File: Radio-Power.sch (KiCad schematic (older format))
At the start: 17 parts, among them J1 Input, J2 Radio Power, Q1 BS170, Q2 FQP27P06, Q3 BS170, U1 L7805, U2 ATtiny85-20PU

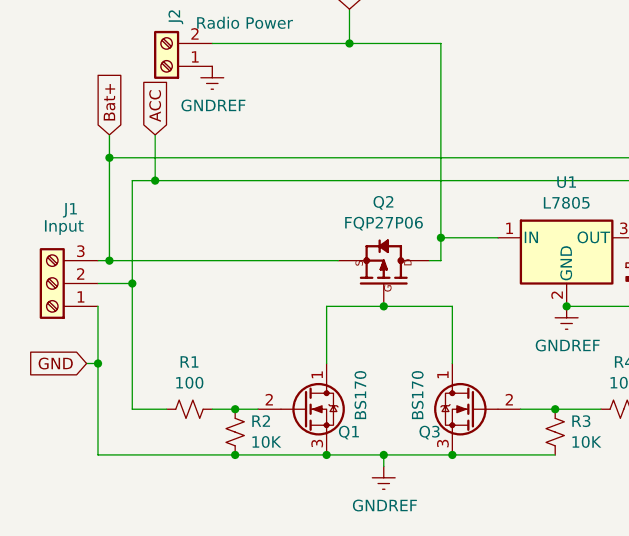
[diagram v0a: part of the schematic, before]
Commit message: Forgot a resistor
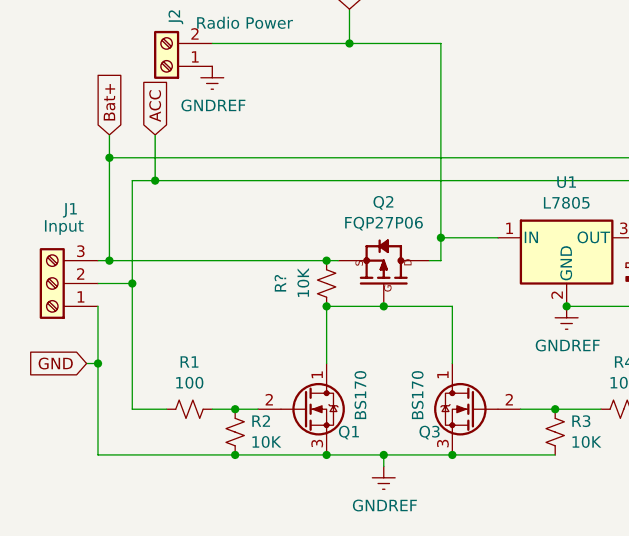
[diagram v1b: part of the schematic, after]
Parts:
- added R?: 10K, Resistor_THT:R_Axial_DIN0207_L6.3mm_D2.5mm_P10.16mm_Horizontal, symbol Device:R_Small_US
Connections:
- net Bat+: now also R?.2
- net at Q1.1 (D), Q2.1 (G), Q3.1 (D): now also R?.1
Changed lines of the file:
@@
 Connection ~ 850  3500
 Wire Wire Line
-	850  3500 1850 3500
+	850  3500 1800 3500
 Wire Wire Line
 	2250 3500 2300 3500
@@
 Wire Wire Line
 	2300 3400 2550 3400
+$Comp
+L Device:R_Small_US R?
+U 1 1 5EABB6D6
+P 1800 3600
+F 0 "R?" V 2000 3600 50  0000 C CNN
+F 1 "10K" V 1900 3600 50  0000 C CNN
+F 2 "Resistor_THT:R_Axial_DIN0207_L6.3mm_D2.5mm_P10.16mm_Horizontal" H 1800 3600 50  0001 C CNN
+F 3 "~" H 1800 3600 50  0001 C CNN
+	1    1800 3600
+	-1   0    0    1
+$EndComp
+Connection ~ 1800 3700
+Connection ~ 1800 3500
+Wire Wire Line
+	1800 3500 1850 3500
 $EndSCHEMATC

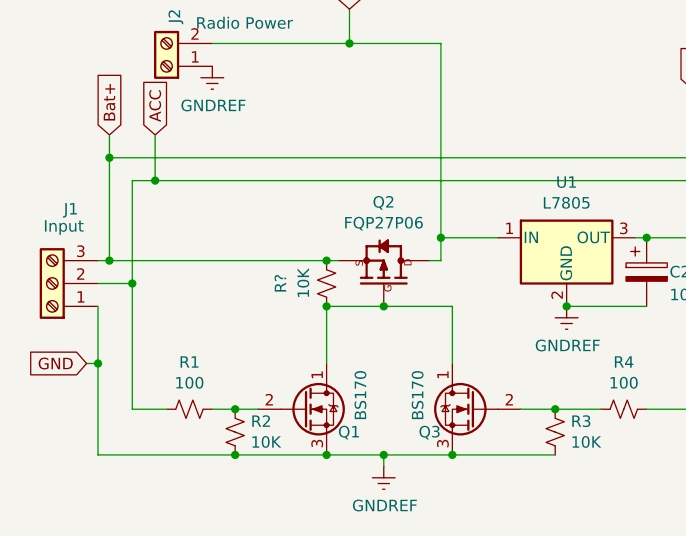
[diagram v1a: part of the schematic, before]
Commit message: Fix rendered schematic
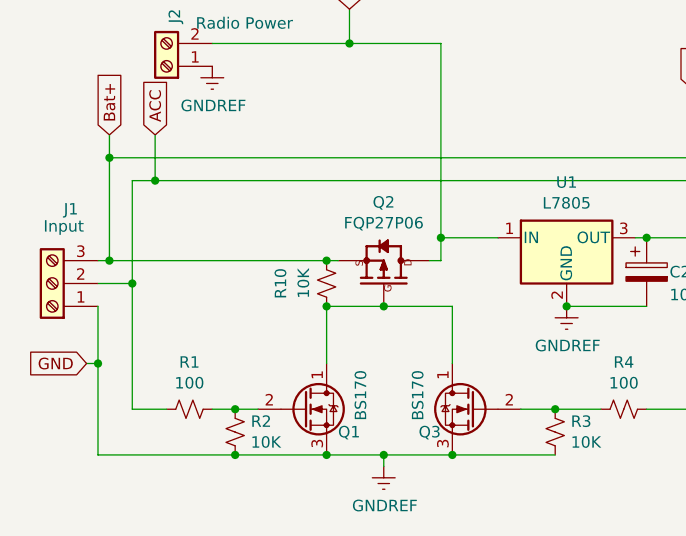
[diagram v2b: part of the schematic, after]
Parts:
- gave numbers to parts that had none: 1
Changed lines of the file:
@@
 	2300 3400 2550 3400
 $Comp
-L Device:R_Small_US R?
+L Device:R_Small_US R10
 U 1 1 5EABB6D6
 P 1800 3600
-F 0 "R?" V 2000 3600 50  0000 C CNN
+F 0 "R10" V 2000 3600 50  0000 C CNN
 F 1 "10K" V 1900 3600 50  0000 C CNN
 F 2 "Resistor_THT:R_Axial_DIN0207_L6.3mm_D2.5mm_P10.16mm_Horizontal" H 1800 3600 50  0001 C CNN

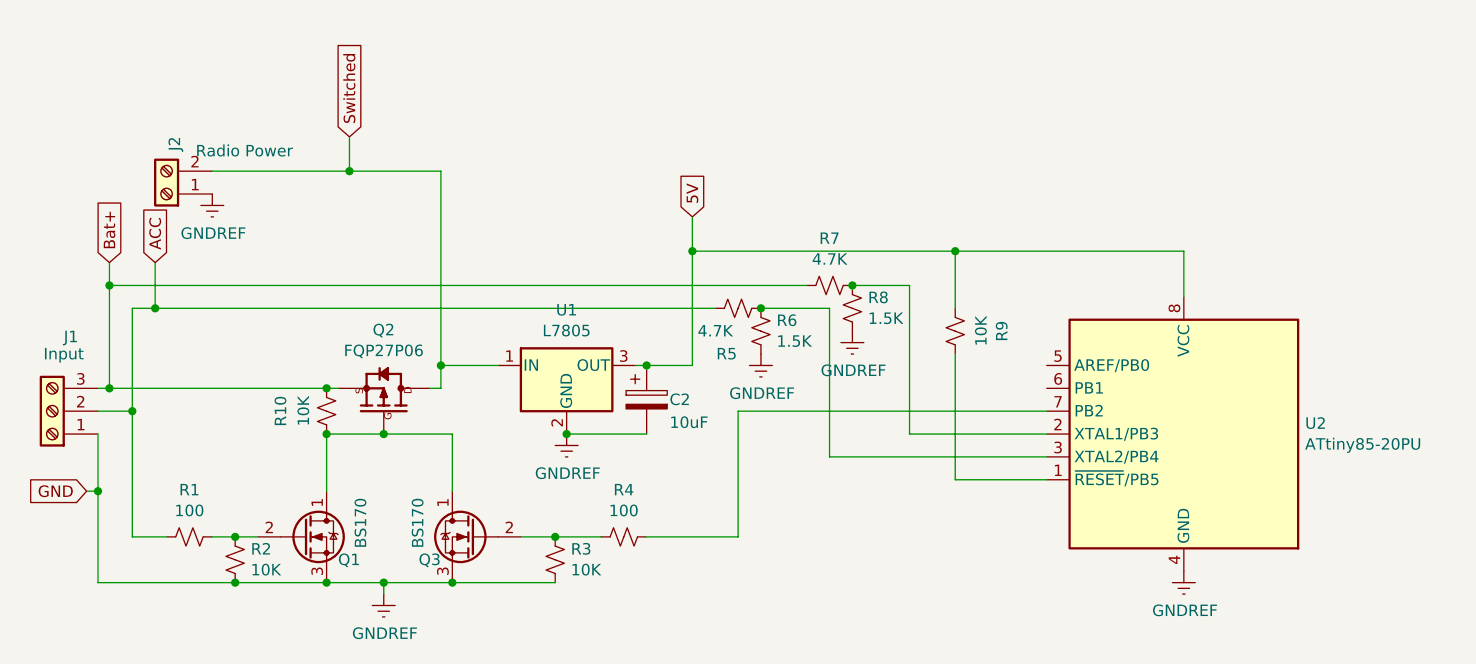
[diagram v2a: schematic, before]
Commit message: Change some things, use switched power for measurement to prevent accidental power flow into the uC
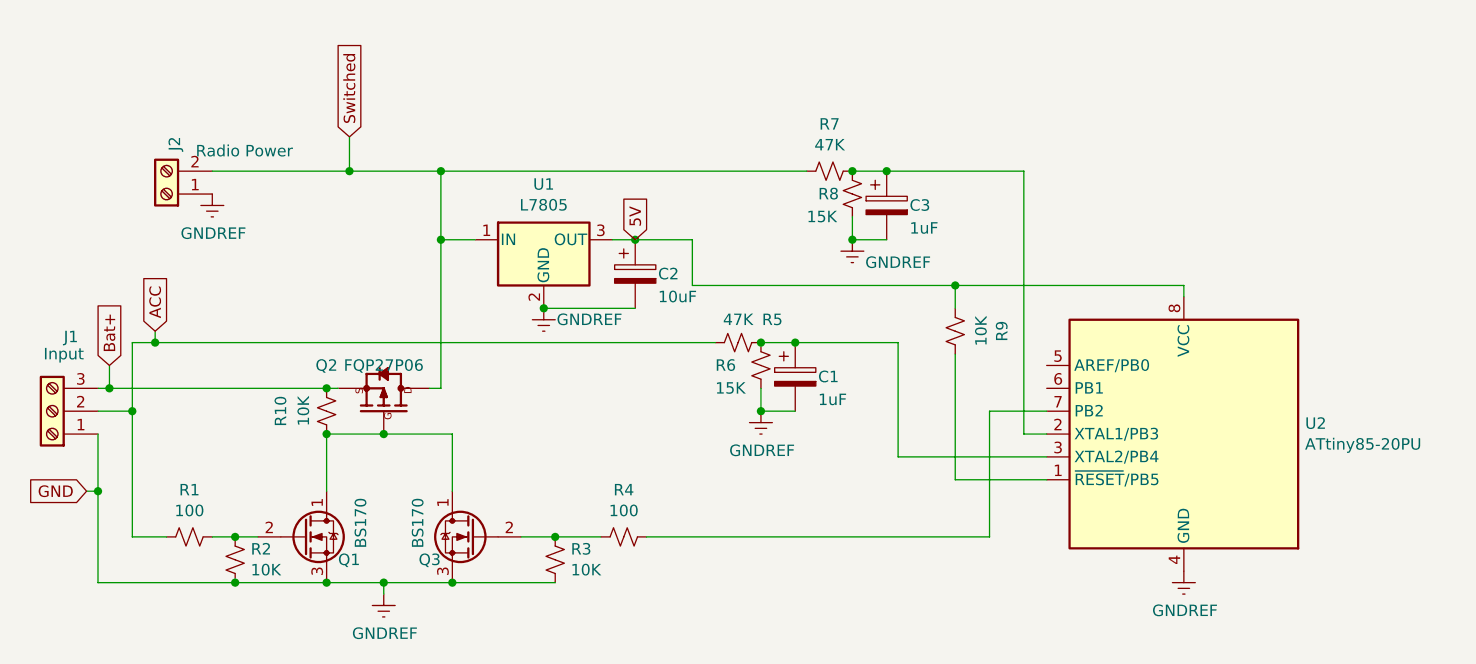
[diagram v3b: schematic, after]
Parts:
- added C1, C3: 1uF, Capacitor_THT:CP_Radial_D4.0mm_P2.00mm, symbol Device:CP
- R5, R7: value 4.7K -> 47K
- R6, R8: value 1.5K -> 15K
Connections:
- net Bat+: no longer R7.2
- net GNDREF: now also C1.2, C3.2
- net Switched: now also R7.2
- net at R7.1, R8.2, U2.2 (XTAL1/PB3): now also C3.1
- net at R5.1, R6.2, U2.3 (XTAL2/PB4): now also C1.1
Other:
- moved on the sheet: C2, R5, R6, R7, R8, U1
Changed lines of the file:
@@
 U 1 1 5EA1FD01
 P 2050 3500
-F 0 "Q2" V 2305 3500 50  0000 C CNN
-F 1 "FQP27P06" V 2214 3500 50  0000 C CNN
+F 0 "Q2" V 2150 3250 50  0000 C CNN
+F 1 "FQP27P06" V 2150 3500 50  0000 C CNN
 F 2 "Package_TO_SOT_THT:TO-220-3_Vertical" H 2050 3500 50  0001 L BNN
 F 3 "67V 27A" H 2050 3500 50  0001 L BNN
@@
 	950  4150 1100 4150
 Wire Wire Line
-	950  3600 950  3150
+	950  3600 950  3300
 Connection ~ 950  3600
-Wire Wire Line
-	850  3500 850  3050
 Connection ~ 850  3500
 Wire Wire Line
@@
 	2250 3500 2300 3500
 Wire Wire Line
-	2300 3500 2300 3400
+	2300 3500 2300 2850
 $Comp
 L MCU_Microchip_ATtiny:ATtiny85-20PU U2
@@
 L Device:R_Small_US R7
 U 1 1 5EA562A8
-P 4000 3050
-F 0 "R7" V 3795 3050 50  0000 C CNN
-F 1 "4.7K" V 3886 3050 50  0000 C CNN
-F 2 "Resistor_THT:R_Axial_DIN0207_L6.3mm_D2.5mm_P10.16mm_Horizontal" H 4000 3050 50  0001 C CNN
-F 3 "~" H 4000 3050 50  0001 C CNN
-	1    4000 3050
+P 4000 2550
+F 0 "R7" V 3795 2550 50  0000 C CNN
+F 1 "47K" V 3886 2550 50  0000 C CNN
+F 2 "Resistor_THT:R_Axial_DIN0207_L6.3mm_D2.5mm_P10.16mm_Horizontal" H 4000 2550 50  0001 C CNN
+F 3 "~" H 4000 2550 50  0001 C CNN
+	1    4000 2550
 	0    1    1    0
 $EndComp
@@
 L Device:R_Small_US R5
 U 1 1 5EA56DEC
-P 3600 3150
-F 0 "R5" V 3800 3100 50  0000 C CNN
-F 1 "4.7K" V 3700 3050 50  0000 C CNN
-F 2 "Resistor_THT:R_Axial_DIN0207_L6.3mm_D2.5mm_P10.16mm_Horizontal" H 3600 3150 50  0001 C CNN
-F 3 "~" H 3600 3150 50  0001 C CNN
-	1    3600 3150
+P 3600 3300
+F 0 "R5" V 3500 3450 50  0000 C CNN
+F 1 "47K" V 3500 3300 50  0000 C CNN
+F 2 "Resistor_THT:R_Axial_DIN0207_L6.3mm_D2.5mm_P10.16mm_Horizontal" H 3600 3300 50  0001 C CNN
+F 3 "~" H 3600 3300 50  0001 C CNN
+	1    3600 3300
 	0    1    1    0
 $EndComp
@@
 L Device:R_Small_US R6
 U 1 1 5EA570DD
-P 3700 3250
-F 0 "R6" H 3632 3204 50  0000 R CNN
-F 1 "1.5K" H 3632 3295 50  0000 R CNN
-F 2 "Resistor_THT:R_Axial_DIN0207_L6.3mm_D2.5mm_P10.16mm_Horizontal" H 3700 3250 50  0001 C CNN
-F 3 "~" H 3700 3250 50  0001 C CNN
-	1    3700 3250
-	-1   0    0    1
-$EndComp
-Wire Wire Line
-	950  3150 1050 3150
-Wire Wire Line
-	850  3050 3900 3050
-Wire Wire Line
-	3700 3150 4000 3150
-Connection ~ 3700 3150
-Wire Wire Line
-	4950 3800 4000 3800
-Wire Wire Line
-	4000 3150 4000 3800
+P 3700 3400
+F 0 "R6" H 3900 3400 50  0000 R CNN
+F 1 "15K" H 3900 3500 50  0000 R CNN
+F 2 "Resistor_THT:R_Axial_DIN0207_L6.3mm_D2.5mm_P10.16mm_Horizontal" H 3700 3400 50  0001 C CNN
+F 3 "~" H 3700 3400 50  0001 C CNN
+	1    3700 3400
+	-1   0    0    1
+$EndComp
+Wire Wire Line
+	950  3300 1050 3300
+Wire Wire Line
+	3700 3300 3850 3300
+Connection ~ 3700 3300
+Wire Wire Line
+	4950 3800 4300 3800
+Wire Wire Line
+	4300 3300 4300 3800
 $Comp
 L Device:R_Small_US R8
 U 1 1 5EA5694E
-P 4100 3150
-F 0 "R8" H 4032 3104 50  0000 R CNN
-F 1 "1.5K" H 4032 3195 50  0000 R CNN
-F 2 "Resistor_THT:R_Axial_DIN0207_L6.3mm_D2.5mm_P10.16mm_Horizontal" H 4100 3150 50  0001 C CNN
-F 3 "~" H 4100 3150 50  0001 C CNN
-	1    4100 3150
-	-1   0    0    1
-$EndComp
-Wire Wire Line
-	4950 3700 4350 3700
-Wire Wire Line
-	4350 3700 4350 3050
-Wire Wire Line
-	4350 3050 4100 3050
-Connection ~ 4100 3050
+P 4100 2650
+F 0 "R8" H 4250 2650 50  0000 R CNN
+F 1 "15K" H 4300 2750 50  0000 R CNN
+F 2 "Resistor_THT:R_Axial_DIN0207_L6.3mm_D2.5mm_P10.16mm_Horizontal" H 4100 2650 50  0001 C CNN
+F 3 "~" H 4100 2650 50  0001 C CNN
+	1    4100 2650
+	-1   0    0    1
+$EndComp
+Wire Wire Line
+	4950 3700 4850 3700
+Wire Wire Line
+	4850 3700 4850 2550
+Wire Wire Line
+	4850 2550 4250 2550
+Connection ~ 4100 2550
 $Comp
 L power:GNDREF #PWR0102
 U 1 1 5EA25084
-P 3700 3350
-F 0 "#PWR0102" H 3700 3100 50  0001 C CNN
-F 1 "GNDREF" H 3705 3177 50  0000 C CNN
-F 2 "" H 3700 3350 50  0001 C CNN
-F 3 "" H 3700 3350 50  0001 C CNN
-	1    3700 3350
+P 3700 3600
+F 0 "#PWR0102" H 3700 3350 50  0001 C CNN
+F 1 "GNDREF" H 3705 3427 50  0000 C CNN
+F 2 "" H 3700 3600 50  0001 C CNN
+F 3 "" H 3700 3600 50  0001 C CNN
+	1    3700 3600
 	1    0    0    -1
 $EndComp
@@
 L power:GNDREF #PWR0103
 U 1 1 5EA2541B
-P 4100 3250
-F 0 "#PWR0103" H 4100 3000 50  0001 C CNN
-F 1 "GNDREF" H 4105 3077 50  0000 C CNN
-F 2 "" H 4100 3250 50  0001 C CNN
-F 3 "" H 4100 3250 50  0001 C CNN
-	1    4100 3250
+P 4100 2850
+F 0 "#PWR0103" H 4100 2600 50  0001 C CNN
+F 1 "GNDREF" H 4300 2750 50  0000 C CNN
+F 2 "" H 4100 2850 50  0001 C CNN
+F 3 "" H 4100 2850 50  0001 C CNN
+	1    4100 2850
 	1    0    0    -1
 $EndComp
@@
 L Regulator_Linear:L7805 U1
 U 1 1 5EA25C90
-P 2850 3400
-F 0 "U1" H 2850 3642 50  0000 C CNN
-F 1 "L7805" H 2850 3551 50  0000 C CNN
-F 2 "Package_TO_SOT_THT:TO-220-3_Vertical" H 2875 3250 50  0001 L CIN
-F 3 "http://www.st.com/content/ccc/resource/technical/document/datasheet/41/4f/b3/b0/12/d4/47/88/CD00000444.pdf/files/CD00000444.pdf/jcr:content/translations/en.CD00000444.pdf" H 2850 3350 50  0001 C CNN
-	1    2850 3400
-	1    0    0    -1
-$EndComp
-Connection ~ 2300 3400
-Wire Wire Line
-	5550 2900 5550 3100
+P 2750 2850
+F 0 "U1" H 2750 3092 50  0000 C CNN
+F 1 "L7805" H 2750 3001 50  0000 C CNN
+F 2 "Package_TO_SOT_THT:TO-220-3_Vertical" H 2775 2700 50  0001 L CIN
+F 3 "http://www.st.com/content/ccc/resource/technical/document/datasheet/41/4f/b3/b0/12/d4/47/88/CD00000444.pdf/files/CD00000444.pdf/jcr:content/translations/en.CD00000444.pdf" H 2750 2800 50  0001 C CNN
+	1    2750 2850
+	1    0    0    -1
+$EndComp
+Connection ~ 2300 2850
+Wire Wire Line
+	5550 3050 5550 3100
 $Comp
 L Device:CP C2
 U 1 1 5EA3195B
-P 3200 3550
-F 0 "C2" H 3300 3550 50  0000 L CNN
-F 1 "10uF" H 3300 3450 50  0000 L CNN
-F 2 "Capacitor_THT:CP_Radial_D10.0mm_P3.50mm" H 3238 3400 50  0001 C CNN
-F 3 "~" H 3200 3550 50  0001 C CNN
-	1    3200 3550
-	1    0    0    -1
-$EndComp
-Wire Wire Line
-	3400 2900 3400 3400
-Wire Wire Line
-	3400 2900 4550 2900
-Connection ~ 2850 3700
-Wire Wire Line
-	2850 3700 3200 3700
+P 3150 3000
+F 0 "C2" H 3250 3000 50  0000 L CNN
+F 1 "10uF" H 3250 2900 50  0000 L CNN
+F 2 "Capacitor_THT:CP_Radial_D10.0mm_P3.50mm" H 3188 2850 50  0001 C CNN
+F 3 "~" H 3150 3000 50  0001 C CNN
+	1    3150 3000
+	1    0    0    -1
+$EndComp
+Wire Wire Line
+	3400 3050 4550 3050
+Connection ~ 2750 3150
+Wire Wire Line
+	2750 3150 3150 3150
 $Comp
 L power:GNDREF #PWR0104
 U 1 1 5EA34E03
-P 2850 3700
-F 0 "#PWR0104" H 2850 3450 50  0001 C CNN
-F 1 "GNDREF" H 2855 3527 50  0000 C CNN
-F 2 "" H 2850 3700 50  0001 C CNN
-F 3 "" H 2850 3700 50  0001 C CNN
-	1    2850 3700
-	1    0    0    -1
-$EndComp
-Connection ~ 3200 3400
-Wire Wire Line
-	3200 3400 3150 3400
-Wire Wire Line
-	3200 3400 3400 3400
-Wire Wire Line
-	4950 3600 3600 3600
-Wire Wire Line
-	3600 3600 3600 4150
-Wire Wire Line
-	3600 4150 3200 4150
-Text GLabel 850  2950 1    50   Input ~ 0
+P 2750 3150
+F 0 "#PWR0104" H 2750 2900 50  0001 C CNN
+F 1 "GNDREF" H 2950 3100 50  0000 C CNN
+F 2 "" H 2750 3150 50  0001 C CNN
+F 3 "" H 2750 3150 50  0001 C CNN
+	1    2750 3150
+	1    0    0    -1
+$EndComp
+Wire Wire Line
+	3150 2850 3050 2850
+Text GLabel 850  3400 1    50   Input ~ 0
 Bat+
-Text GLabel 1050 2950 1    50   Input ~ 0
+Text GLabel 1050 3250 1    50   Input ~ 0
 ACC
 Wire Wire Line
-	1050 3150 1050 2950
-Connection ~ 1050 3150
-Wire Wire Line
-	1050 3150 3500 3150
-Wire Wire Line
-	850  2950 850  3050
-Connection ~ 850  3050
+	1050 3300 1050 3250
+Connection ~ 1050 3300
+Wire Wire Line
+	1050 3300 3500 3300
 Text GLabel 750  3950 0    50   Input ~ 0
 GND
@@
 Wire Wire Line
 	2300 2550 1900 2550
-Wire Wire Line
-	2300 2550 2300 3400
 Text GLabel 1900 2400 1    50   Input ~ 0
 Switched
@@
 	-1   0    0    1
 $EndComp
-Text GLabel 3400 2750 1    50   Input ~ 0
+Text GLabel 3150 2850 1    50   Input ~ 0
 5V
 Wire Wire Line
-	3400 2900 3400 2750
-Connection ~ 3400 2900
-Wire Wire Line
-	4550 3150 4550 2900
-Connection ~ 4550 2900
-Wire Wire Line
-	4550 2900 5550 2900
+	4550 3150 4550 3050
+Connection ~ 4550 3050
+Wire Wire Line
+	4550 3050 5550 3050
 Wire Wire Line
 	4550 3350 4550 3900
@@
 	2050 3700 2350 3700
 Wire Wire Line
-	2300 3400 2550 3400
+	2300 2850 2450 2850
 $Comp
 L Device:R_Small_US R10
@@
 Wire Wire Line
 	1800 3500 1850 3500
+Wire Wire Line
+	850  3400 850  3500
+Wire Wire Line
+	3900 2550 2300 2550
+Connection ~ 2300 2550
+Wire Wire Line
+	2300 2550 2300 2850
+$Comp
+L Device:CP C3
+U 1 1 5EA3F089
+P 4250 2700
+F 0 "C3" H 4350 2700 50  0000 L CNN
+F 1 "1uF" H 4350 2600 50  0000 L CNN
+F 2 "Capacitor_THT:CP_Radial_D4.0mm_P2.00mm" H 4288 2550 50  0001 C CNN
+F 3 "~" H 4250 2700 50  0001 C CNN
+	1    4250 2700
+	1    0    0    -1
+$EndComp
+Connection ~ 4250 2550
+Wire Wire Line
+	4250 2550 4100 2550
+Wire Wire Line
+	4100 2750 4100 2850
+Wire Wire Line
+	4250 2850 4100 2850
+Connection ~ 4100 2850
+Wire Wire Line
+	3150 2850 3400 2850
+Connection ~ 3150 2850
+Wire Wire Line
+	3400 2850 3400 3050
+$Comp
+L Device:CP C1
+U 1 1 5EA99D67
+P 3850 3450
+F 0 "C1" H 3950 3450 50  0000 L CNN
+F 1 "1uF" H 3950 3350 50  0000 L CNN
+F 2 "Capacitor_THT:CP_Radial_D4.0mm_P2.00mm" H 3888 3300 50  0001 C CNN
+F 3 "~" H 3850 3450 50  0001 C CNN
+	1    3850 3450
+	1    0    0    -1
+$EndComp
+Wire Wire Line
+	3700 3500 3700 3600
+Wire Wire Line
+	3700 3600 3850 3600
+Connection ~ 3700 3600
+Connection ~ 3850 3300
+Wire Wire Line
+	3850 3300 4300 3300
+Wire Wire Line
+	4700 4150 4700 3600
+Wire Wire Line
+	4700 3600 4950 3600
+Wire Wire Line
+	3200 4150 4700 4150
 $EndSCHEMATC

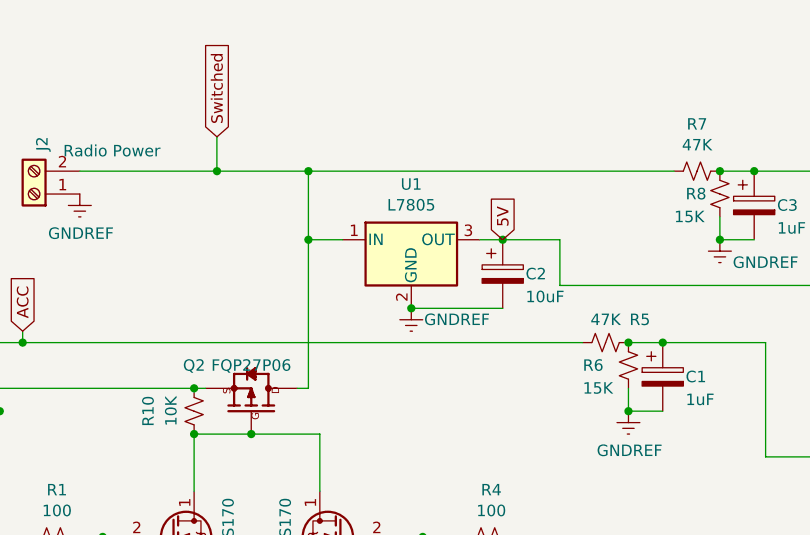
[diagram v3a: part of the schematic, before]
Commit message: Minor updates, add a cap and move the regulator
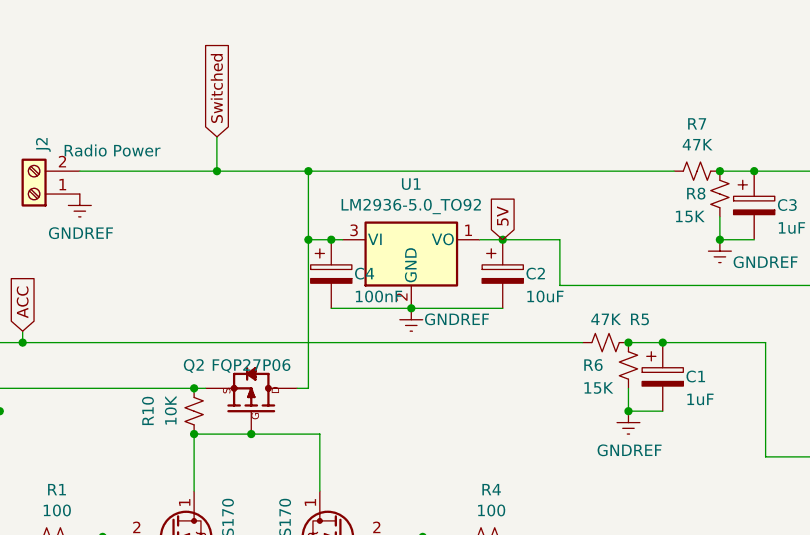
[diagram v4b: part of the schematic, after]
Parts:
- removed U1: L7805, Package_TO_SOT_THT:TO-220-3_Vertical, symbol Regulator_Linear:L7805
- added C4: 100nF, Capacitor_THT:C_Disc_D3.0mm_W2.0mm_P2.50mm, symbol Device:CP
- added U1: LM2936-5.0_TO92, Package_TO_SOT_THT:TO-92_Inline, symbol Regulator_Linear:LM2936-5.0_TO92
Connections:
- net 5V: now also U1.1 (VO)
- net GNDREF: now also C4.2, U1.2 (GND)
- net Switched: now also C4.1, U1.3 (VI)
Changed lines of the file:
@@
-	1    0    0    -1
-$EndComp
-$Comp
-L Regulator_Linear:L7805 U1
-U 1 1 5EA25C90
-P 2750 2850
-F 0 "U1" H 2750 3092 50  0000 C CNN
-F 1 "L7805" H 2750 3001 50  0000 C CNN
-F 2 "Package_TO_SOT_THT:TO-220-3_Vertical" H 2775 2700 50  0001 L CIN
-F 3 "http://www.st.com/content/ccc/resource/technical/document/datasheet/41/4f/b3/b0/12/d4/47/88/CD00000444.pdf/files/CD00000444.pdf/jcr:content/translations/en.CD00000444.pdf" H 2750 2800 50  0001 C CNN
-	1    2750 2850
 	1    0    0    -1
 $EndComp
@@
 	2050 3700 2350 3700
 Wire Wire Line
-	2300 2850 2450 2850
+	2300 2850 2400 2850
 $Comp
 L Device:R_Small_US R10
@@
 Wire Wire Line
 	3200 4150 4700 4150
+$Comp
+L Regulator_Linear:LM2936-5.0_TO92 U1
+U 1 1 5EA4721F
+P 2750 2850
+F 0 "U1" H 2750 3092 50  0000 C CNN
+F 1 "LM2936-5.0_TO92" H 2750 3001 50  0000 C CNN
+F 2 "Package_TO_SOT_THT:TO-92_Inline" H 2750 3075 50  0001 C CIN
+F 3 "http://www.ti.com/lit/ds/symlink/lm2936.pdf" H 2750 2800 50  0001 C CNN
+	1    2750 2850
+	1    0    0    -1
+$EndComp
+$Comp
+L Device:CP C4
+U 1 1 5EA5B7CA
+P 2400 3000
+F 0 "C4" H 2500 3000 50  0000 L CNN
+F 1 "100nF" H 2500 2900 50  0000 L CNN
+F 2 "Capacitor_THT:C_Disc_D3.0mm_W2.0mm_P2.50mm" H 2438 2850 50  0001 C CNN
+F 3 "~" H 2400 3000 50  0001 C CNN
+	1    2400 3000
+	1    0    0    -1
+$EndComp
+Connection ~ 2400 2850
+Wire Wire Line
+	2400 2850 2450 2850
+Wire Wire Line
+	2400 3150 2750 3150
 $EndSCHEMATC
